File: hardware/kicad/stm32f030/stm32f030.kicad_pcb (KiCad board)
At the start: 2 copper layers, 67.3 x 68.6 mm, 112 parts, among them K1 RELAY_1RT, K2 RELAY_1RT, P1 5VIN, P10 SWD, P2 LOOP1, P3 LOOP2, P4 RELAY OUT 1, P5 TTL OUT 1, P6 RELAY OUT 2, P7 TTL OUT 2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

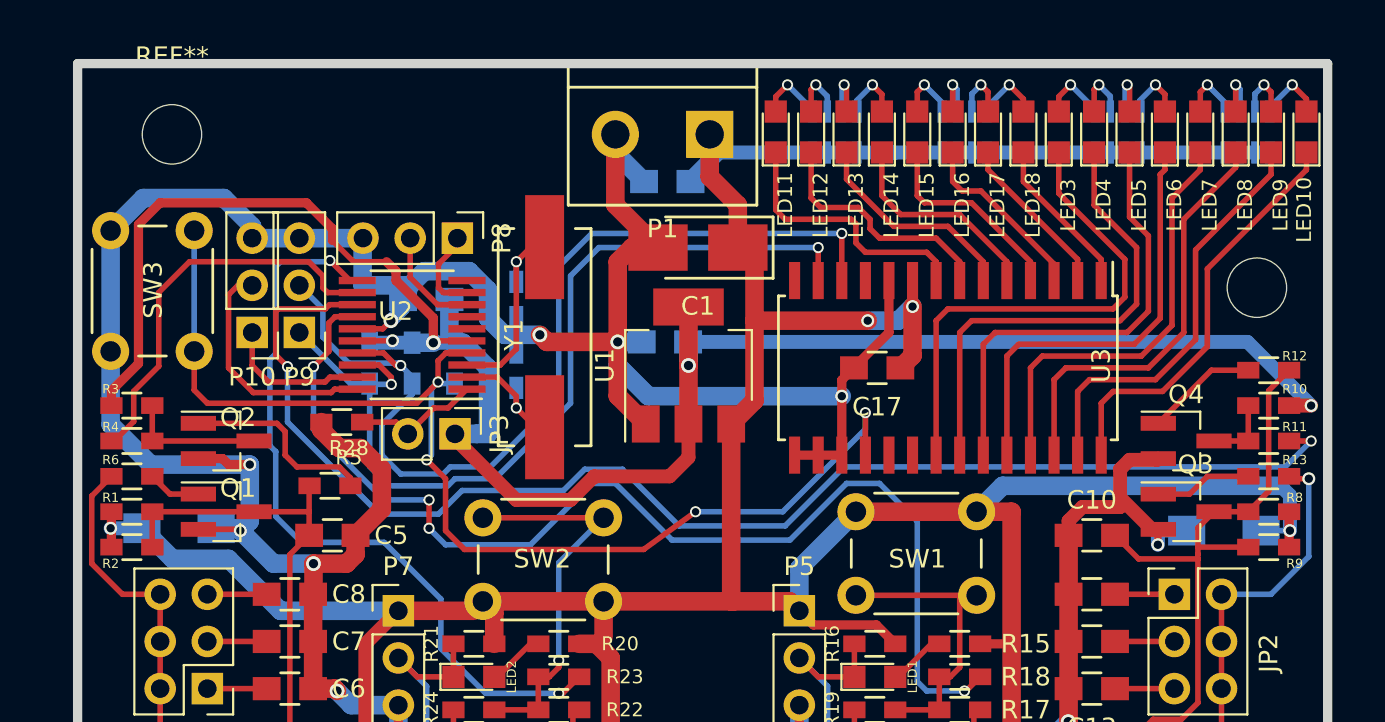
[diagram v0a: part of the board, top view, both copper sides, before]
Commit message: hardware/kicad/stm32f030: adding eeprom step1
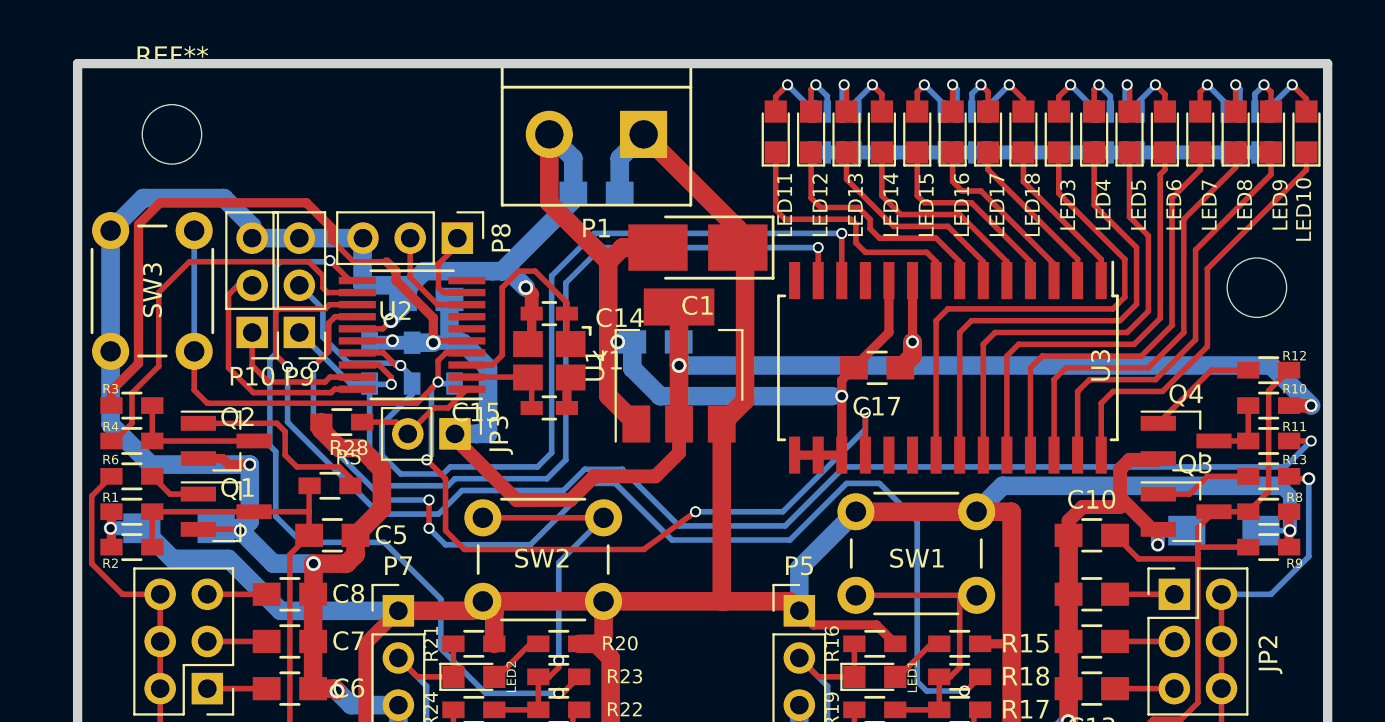
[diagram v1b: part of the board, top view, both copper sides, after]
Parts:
- C14, C15: moved to F.Cu
- RN1, RN2, RN3, RN4: value 330 -> 220
- Y1: value 8MHz -> 12MHz; footprint Crystals:Crystal_HC49-SD_SMD -> Crystals:Crystal_SMD_3225_4Pads
- moved C2 3.86 mm to (63.5, 99.7)
- moved P1 3.56 mm to (63.5, 96.5)
- moved C15 2.70 mm to (61.0, 111.3), turned to 0 degrees
- moved C14 1.93 mm to (61.0, 106.2), turned to 180 degrees
- moved Y1 1.30 mm to (61.0, 108.7), turned to 180 degrees
- moved C3 0.51 mm to (66.7, 107.7)
- moved U1 0.51 mm to (67.9, 109.0)
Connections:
- C17 pad 1: +5V -> +3V3
- RN1 pad 5: +5V -> +3V3
- RN1 pad 6: +5V -> +3V3
- RN1 pad 7: +5V -> +3V3
- RN1 pad 8: +5V -> +3V3
- RN2 pad 5: +5V -> +3V3
- RN2 pad 6: +5V -> +3V3
- RN2 pad 7: +5V -> +3V3
- RN2 pad 8: +5V -> +3V3
- RN3 pad 5: +5V -> +3V3
- RN3 pad 6: +5V -> +3V3
- RN3 pad 7: +5V -> +3V3
- RN3 pad 8: +5V -> +3V3
- RN4 pad 5: +5V -> +3V3
- RN4 pad 6: +5V -> +3V3
- RN4 pad 7: +5V -> +3V3
- RN4 pad 8: +5V -> +3V3
- U3 pad 9: +5V -> +3V3
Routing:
- net +5V: track 218.2 -> 175.0 mm, vias 4 -> 2
- net +3V3: track 110.6 -> 141.0 mm, vias 4 -> 5
- net Net-(C15-Pad1): track 7.37 -> 5.02 mm, vias 1 -> 0
- net GND: track 234.0 -> 236.3 mm, vias 10 -> 9
- net /MCU/sda: track 49.3 -> 50.8 mm
- net Net-(C14-Pad1): track 11.1 -> 12.6 mm, vias 1 -> 0
- net /MCU/scl: track 53.9 -> 55.3 mm
- net (no net): vias 0 -> 1

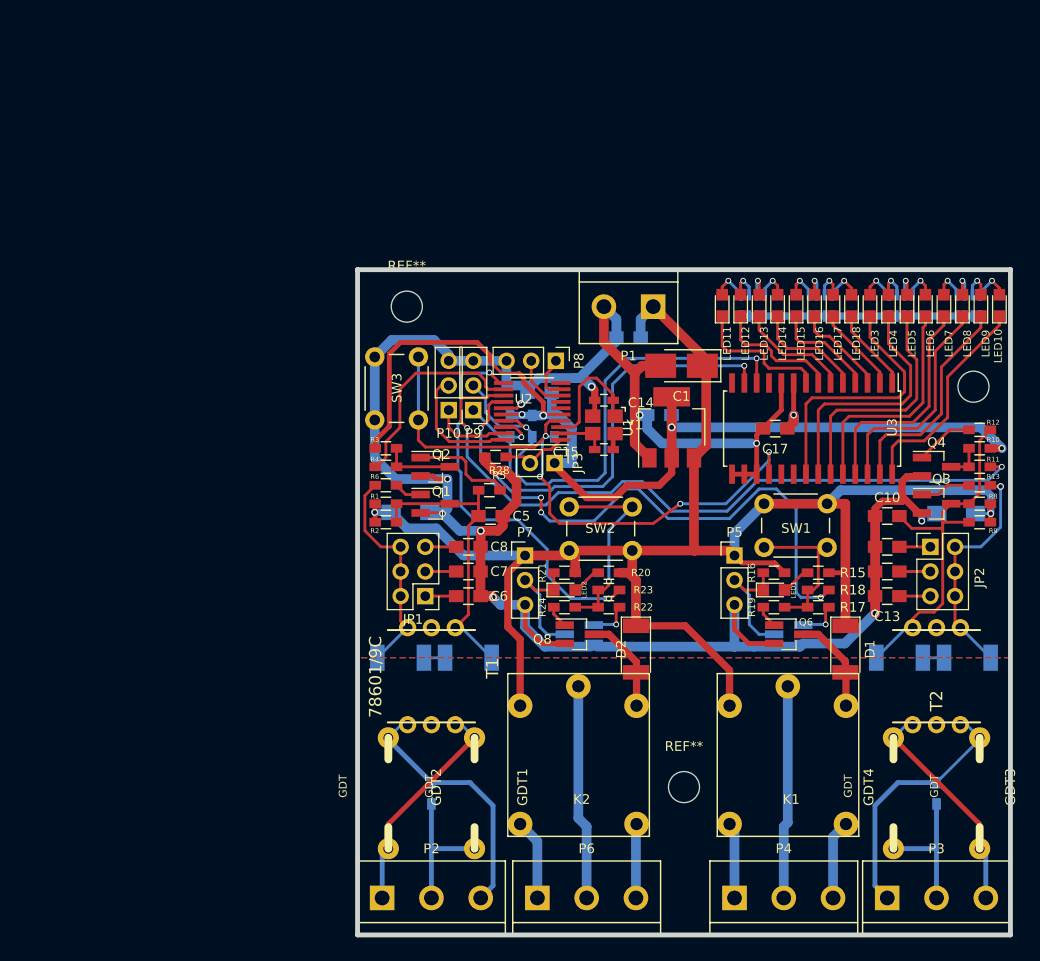
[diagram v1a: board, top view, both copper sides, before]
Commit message: hardware/kicad/stm32f030: adding eeprom step2
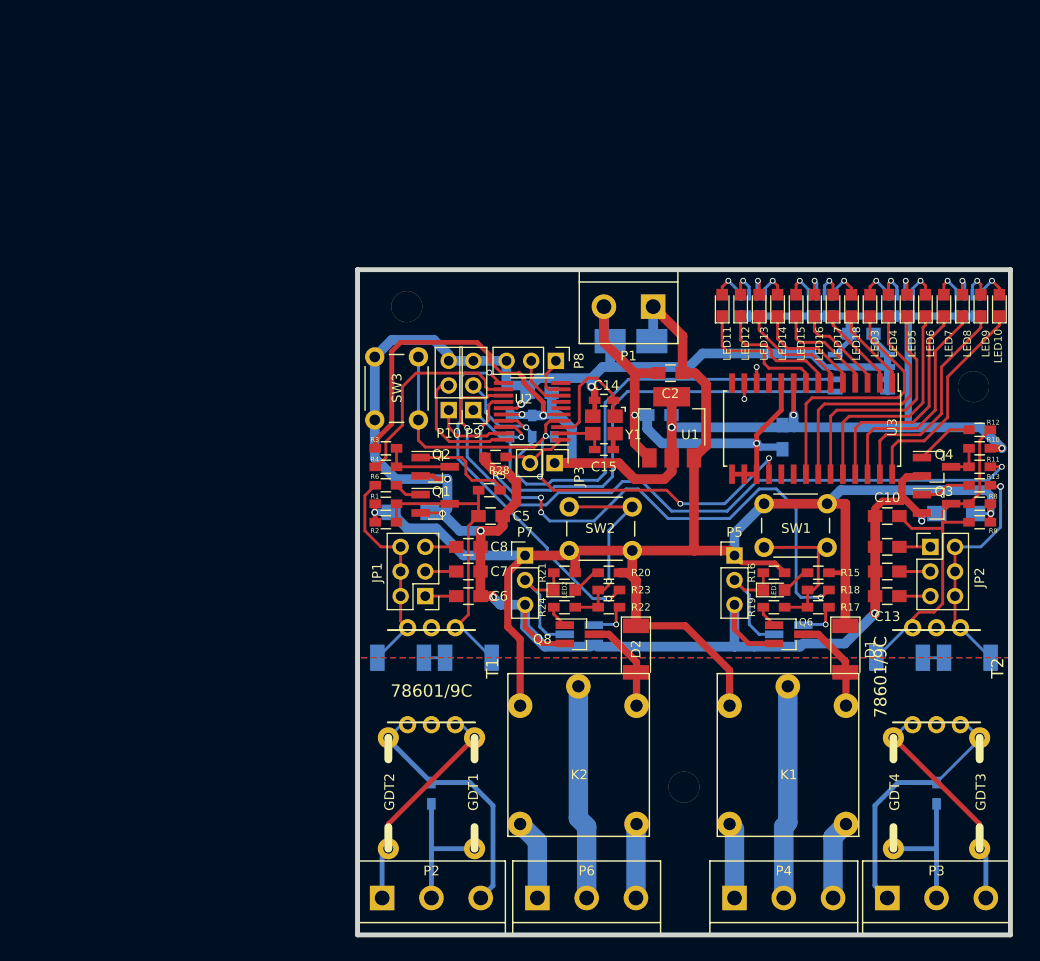
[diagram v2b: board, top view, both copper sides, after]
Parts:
- added C18: 100n, Capacitors_SMD:C_0805_HandSoldering, B.Cu at (87.5, 99.3)
- added IC1: AT24CS02-SSHM, Housings_SOIC:SOIC-8_3.9x4.9mm_Pitch1.27mm, B.Cu at (87.5, 103.4)
- C1, C17: moved to B.Cu
- C2: moved to F.Cu
- GDT1, GDT2, GDT3, GDT4: footprint gdt:CG5350L -> cardetector:GDT
- K1, K2: footprint relays:SRD-SL-C -> cardetector:SRD-SL-C
- T1, T2: footprint murata_pwr:78601_9C -> cardetector:78601_9C
- moved C1 5.79 mm to (63.8, 100.1)
- moved C2 5.68 mm to (67.8, 103.4)
- moved C17 1.17 mm to (79.4, 110.0), turned to 270 degrees
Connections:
- net /MCU/scl renamed /EEPROM/scl
- net /MCU/sda renamed /EEPROM/sda
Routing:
- net GND: track 236.3 -> 274.5 mm, vias 9 -> 10
- net +3V3: track 141.0 -> 154.2 mm
- net /EEPROM/sda: track 50.8 -> 58.4 mm
- net /EEPROM/scl: track 55.3 -> 61.5 mm
- net /MCU/reset: track 63.7 -> 59.2 mm
- net /MCU/active1: track 40.9 -> 36.9 mm
- net +5V: track 175.0 -> 175.6 mm
- net (no net): vias 1 -> 0

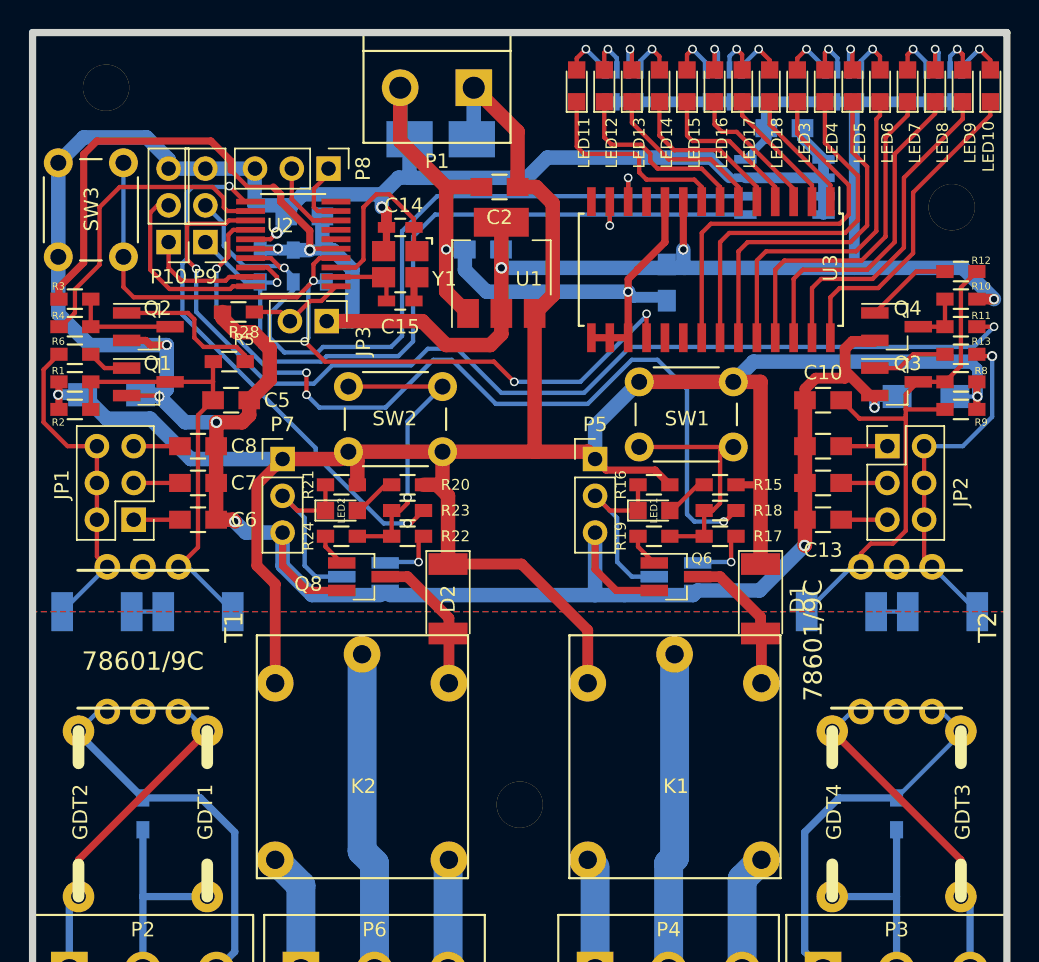
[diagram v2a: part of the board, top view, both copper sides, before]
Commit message: hardware/kicad/stm32f030: adding eeprom step3
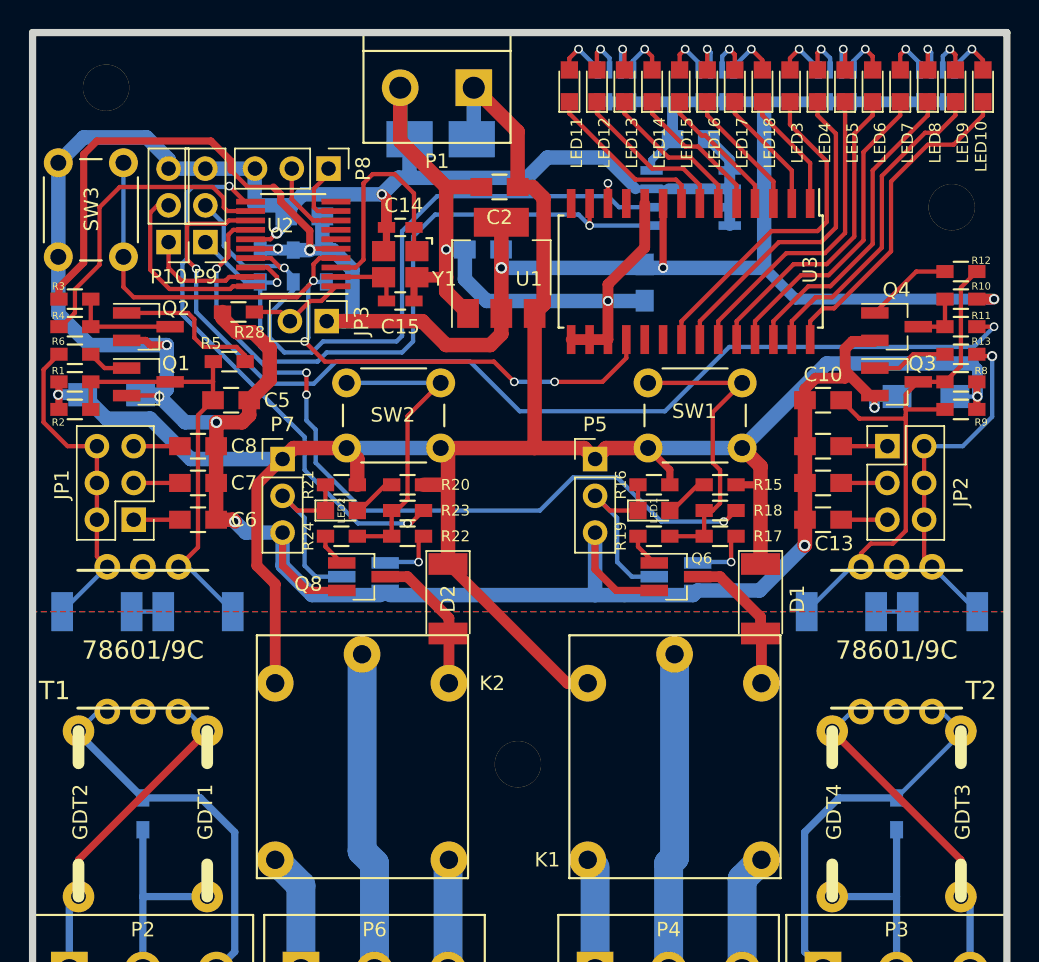
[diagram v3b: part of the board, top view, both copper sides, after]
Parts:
- moved SW1 8.45 mm to (84.6, 121.4), turned to 180 degrees
- moved C18 6.52 mm to (81.0, 100.1)
- moved IC1 6.52 mm to (81.0, 104.1)
- moved REF** 2.80 mm to (69.1, 143.3)
- moved C17 1.52 mm to (77.9, 110.0)
- moved U3 1.40 mm to (81.0, 109.2)
- moved LED10 0.51 mm to (101.2, 96.4)
- moved LED13 0.51 mm to (76.5, 96.4)
- moved LED14 0.51 mm to (78.4, 96.4)
- moved LED15 0.51 mm to (80.3, 96.4)
- moved LED16 0.51 mm to (82.2, 96.4)
- moved LED9 0.51 mm to (99.3, 96.4)
- moved RN2 0.51 mm to (98.0, 96.4)
- moved LED11 0.51 mm to (72.6, 96.4)
- moved LED12 0.51 mm to (74.5, 96.4)
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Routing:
- net +5V: track 175.6 -> 163.8 mm
- net /EEPROM/sda: track 58.4 -> 51.3 mm
- net /EEPROM/scl: track 61.5 -> 54.7 mm
- net /outputs/active1: track 61.0 -> 55.0 mm
- net Net-(R17-Pad2): track 15.8 -> 21.3 mm
- net GND: track 274.5 -> 269.2 mm
- net Net-(LED3-Pad1): track 27.2 -> 23.5 mm
- net Net-(LED4-Pad1): track 25.9 -> 22.6 mm
- net Net-(C14-Pad1): track 12.6 -> 15.8 mm
- net /MCU/reset: track 59.2 -> 56.1 mm
- net Net-(LED5-Pad1): track 24.6 -> 21.6 mm
- net Net-(LED11-Pad1): track 14.5 -> 11.9 mm
- net Net-(LED12-Pad1): track 13.2 -> 11.2 mm
- net Net-(LED6-Pad1): track 23.5 -> 21.7 mm
- net Net-(LED14-Pad1): track 11.5 -> 9.97 mm
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
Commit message: hardware/kicad/stm32f030: final touches
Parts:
- D1, D2, ZD1, ZD2, ZD3, ZD4: footprint Diodes_SMD:MELF_Standard -> Diodes_SMD:D_MiniMELF_Standard
- Q1, Q2, Q3, Q4: footprint TO_SOT_Packages_SMD:SOT-23_Handsoldering -> TO_SOT_Packages_SMD:SOT-23
- R1, R2, R8, R9: footprint Resistors_SMD:R_0603_HandSoldering -> Resistors_SMD:R_0805
- T1, T2: footprint cardetector:78601_9C -> cardetector:Murata_Impulse_Transformer
- moved REF** 1.53 mm to (69.2, 144.8)
- moved ZD1 1.02 mm to (46.0, 132.6)
- moved ZD3 1.02 mm to (92.5, 132.6)
- moved P6 0.99 mm to (58.4, 158.1), turned to 180 degrees
- moved P4 0.81 mm to (80.0, 158.1), turned to 180 degrees
- moved R8 0.81 mm to (99.1, 116.3)
- moved R9 0.74 mm to (99.1, 118.4)
- moved Q4 0.72 mm to (94.7, 112.5)
- moved R1 0.68 mm to (39.1, 116.6)
- moved R13 0.65 mm to (99.6, 114.3)
- moved R2 0.65 mm to (39.1, 118.6)
- moved K1 0.64 mm to (74.0, 150.5)
- moved K2 0.64 mm to (52.4, 150.5)
- moved P2 0.64 mm to (43.2, 158.1), turned to 180 degrees
- moved P3 0.64 mm to (95.2, 158.1), turned to 180 degrees
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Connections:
- P1 pad 1: +5V -> GND
- P1 pad 2: GND -> +5V
- P2 pad 1: Net-(GDT1-Pad1) -> Net-(GDT2-Pad1)
- P2 pad 3: Net-(GDT2-Pad1) -> Net-(GDT1-Pad1)
- P3 pad 1: Net-(GDT3-Pad1) -> Net-(GDT3-Pad2)
- P3 pad 3: Net-(GDT3-Pad2) -> Net-(GDT3-Pad1)
- P4 pad 1: Net-(K1-Pad3) -> Net-(K1-Pad4)
- P4 pad 3: Net-(K1-Pad4) -> Net-(K1-Pad3)
- P6 pad 1: Net-(K2-Pad3) -> Net-(K2-Pad4)
- P6 pad 3: Net-(K2-Pad4) -> Net-(K2-Pad3)
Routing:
- net +5V: track 163.8 -> 169.3 mm
- net GND: track 269.2 -> 266.0 mm
- net Net-(C5-Pad1): track 30.6 -> 29.1 mm
- net Net-(Q2-Pad1): track 10.6 -> 9.08 mm
- net Net-(GDT3-Pad1): track 26.4 -> 27.7 mm
- net Net-(GDT2-Pad1): track 26.4 -> 27.6 mm
- net Net-(C10-Pad1): track 38.4 -> 37.3 mm
- net Net-(GDT4-Pad2): track 14.1 -> 15.2 mm
- net Net-(GDT1-Pad2): track 14.1 -> 15.2 mm
- net Net-(JP1-Pad2): track 23.5 -> 22.5 mm
- net Net-(Q4-Pad3): track 3.75 -> 4.50 mm
- net Net-(Q2-Pad3): track 7.38 -> 6.74 mm
- net Net-(Q1-Pad1): track 2.88 -> 3.41 mm
- net Net-(D2-Pad2): track 10.1 -> 10.6 mm
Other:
- board size 67.3 x 68.6 mm -> 67.3 x 69.2 mm

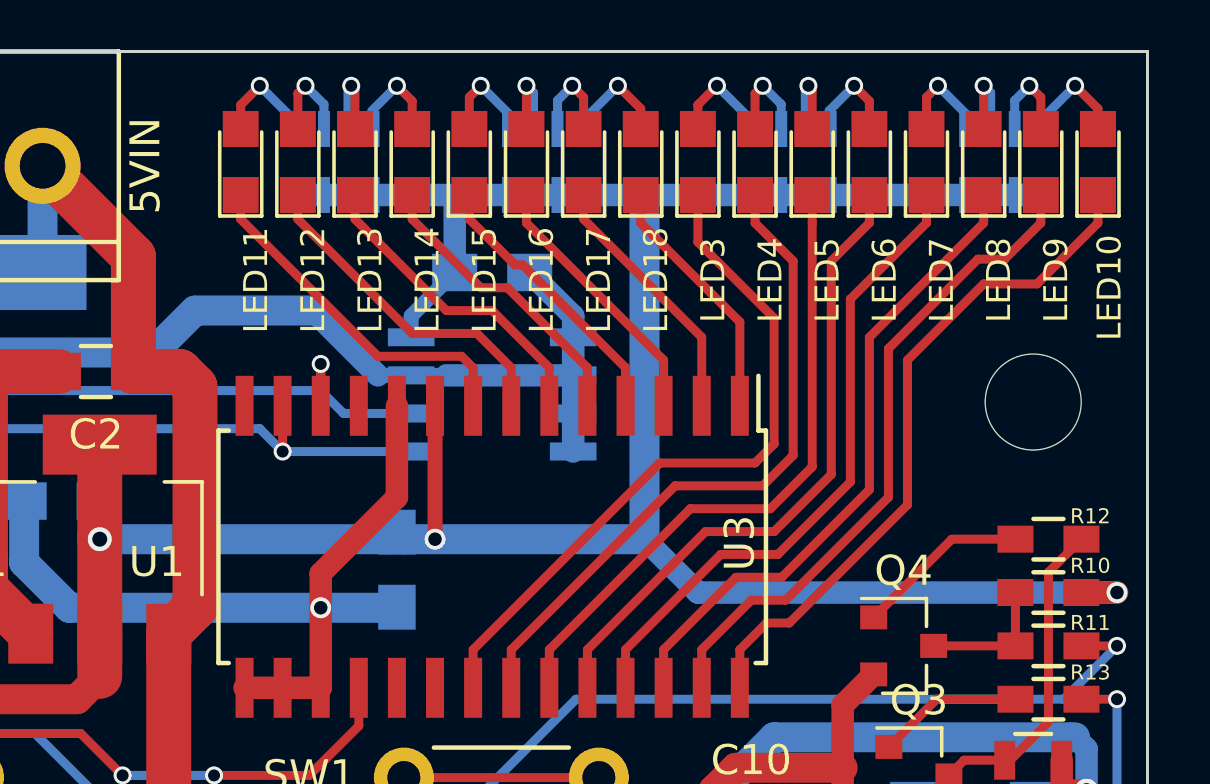
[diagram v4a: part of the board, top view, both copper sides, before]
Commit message: hardware/kicad/stm32f030: i2c eeprom pad widening
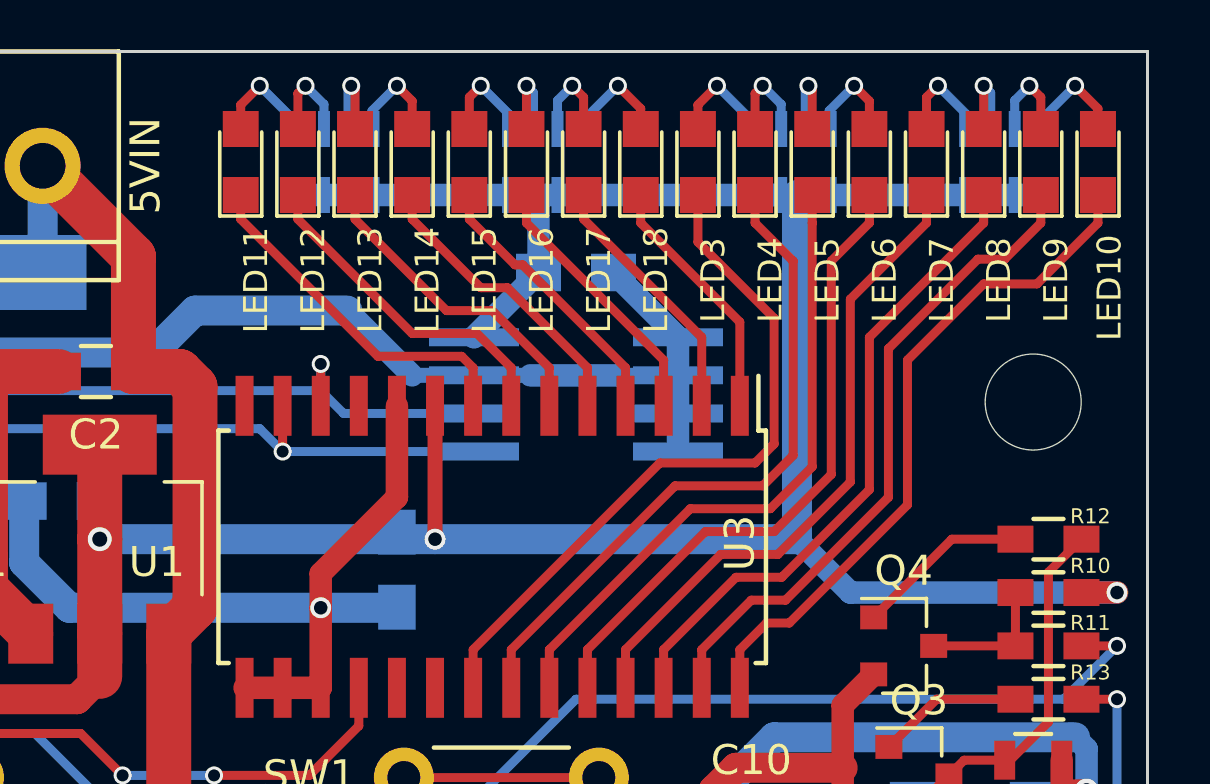
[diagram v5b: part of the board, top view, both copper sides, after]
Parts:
- moved C18 2.79 mm to (83.8, 100.1)
- moved IC1 2.79 mm to (83.8, 104.1)
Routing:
- net GND: track 266.0 -> 272.5 mm
- net /EEPROM/sda: track 51.3 -> 53.4 mm
- net /EEPROM/scl: track 54.7 -> 56.8 mm
- net +3V3: track 154.9 -> 155.9 mm
